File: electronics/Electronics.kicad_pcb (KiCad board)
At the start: 4 copper layers, 102.4 x 75 mm, 85 parts, among them J10 215079-4, J11 215079-4, J12 215079-4, J15 FTSH-105-XX-X-DV, J16 10118193-0001LF, J2 3mm_pad, J4 3mm_pad, J7 215079-4, J8 215079-4, J9 215079-4, Q1 BUK6Y10-30P, U1 STM32G441KBT3, U10 CM1223-02SO, U2 MAX14930DASE+, U3 MAX14930DASE+, U4 MAX14930DASE+, U5 DRV8243, U6 DRV8243, U7 DRV8243, U8 TPS54227DDAR, U9 NCP164

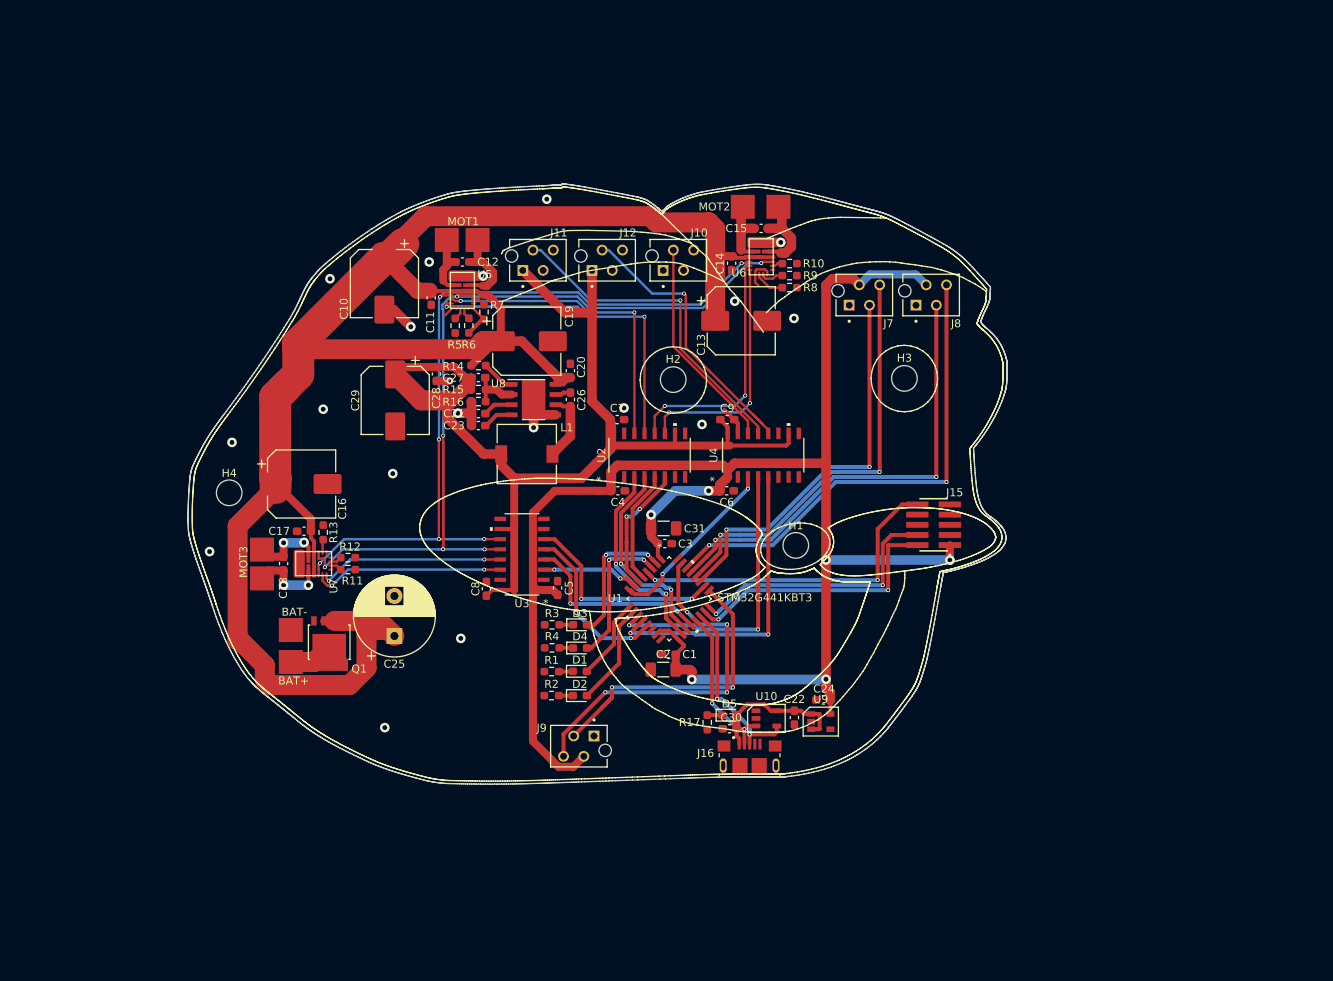
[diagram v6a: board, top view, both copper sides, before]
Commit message: Filled empty areas
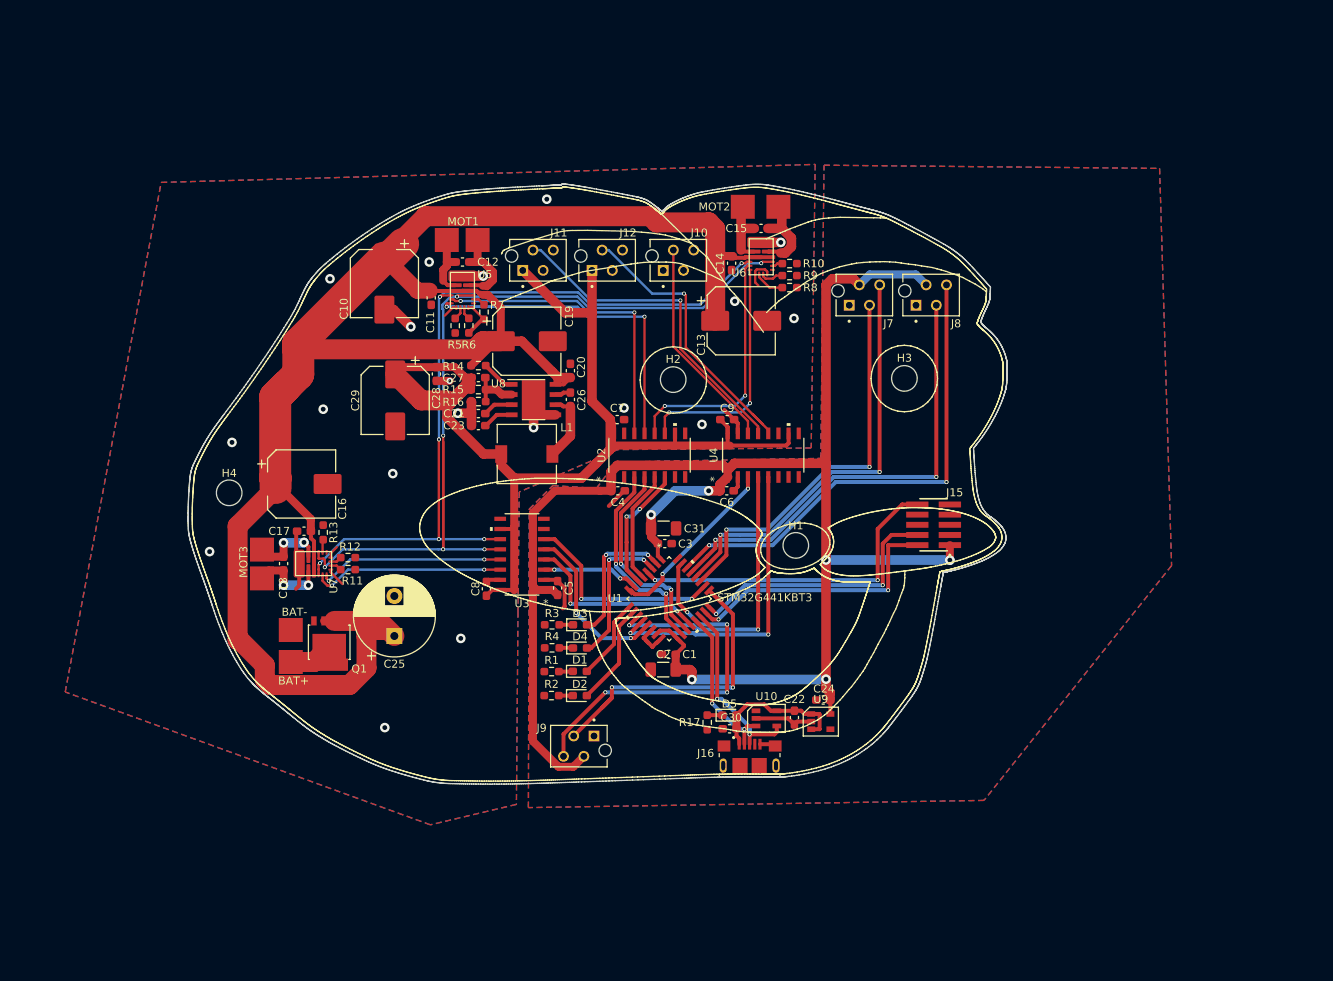
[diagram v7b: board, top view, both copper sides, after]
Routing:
- net GND: track 0.00 -> 24.6 mm
- net Earth: track 37.2 -> 50.6 mm
- added copper zone on B.Cu, net Earth
- added copper zone on F.Cu, net Earth
- added copper zone on B.Cu, net GND
- added copper zone on F.Cu, net GND
- added copper zone on In1.Cu, net GND
- added copper zone on In2.Cu, net GND
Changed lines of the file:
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@@
     (thickness 1.6)
     (drawings 11406)
-    (tracks 836)
+    (tracks 872)
     (zones 0)
     (modules 85)
@@
     (0 F.Cu signal)
     (1 In1.Cu signal)
-    (2 In2.Cu signal hide)
+    (2 In2.Cu signal)
     (31 B.Cu signal)
     (32 B.Adhes user)
@@
   (segment (start 70.284991 76.065009) (end 70.284991 72.265009) (width 4) (layer F.Cu) (net 1))
   (segment (start 67.4 78.95) (end 70.284991 76.065009) (width 4) (layer F.Cu) (net 1))
+  (segment (start 102.5375 101.775) (end 102.7 101.9375) (width 0.5) (layer F.Cu) (net 2))
+  (segment (start 100.974752 101.775) (end 102.5375 101.775) (width 0.5) (layer F.Cu) (net 2))
+  (segment (start 102.7 101.9375) (end 103.577008 102.814508) (width 0.5) (layer F.Cu) (net 2))
+  (segment (start 103.577008 102.814508) (end 103.577008 105.122992) (width 0.5) (layer F.Cu) (net 2))
+  (segment (start 103.577008 105.122992) (end 103.35 105.35) (width 0.5) (layer F.Cu) (net 2))
+  (segment (start 111.1 90.65) (end 111 90.65) (width 0.5) (layer F.Cu) (net 2))
+  (segment (start 111 90.65) (end 109.1 92.55) (width 0.5) (layer F.Cu) (net 2))
+  (segment (start 114.476672 108.020384) (end 113.45 109.047056) (width 0.5) (layer F.Cu) (net 2))
+  (segment (start 114.023526 109.620582) (end 114.023526 109.623526) (width 0.5) (layer F.Cu) (net 2))
+  (segment (start 115.139214 109.620582) (end 115.079418 109.620582) (width 0.5) (layer F.Cu) (net 2))
+  (segment (start 115.608042 109.151754) (end 115.139214 109.620582) (width 0.5) (layer F.Cu) (net 2))
+  (segment (start 115.079418 109.620582) (end 114.55 110.15) (width 0.5) (layer F.Cu) (net 2))
+  (segment (start 114.55 110.147056) (end 113.751472 109.348528) (width 0.5) (layer F.Cu) (net 2))
+  (segment (start 114.55 110.15) (end 114.55 110.147056) (width 0.5) (layer F.Cu) (net 2))
+  (segment (start 113.751472 109.348528) (end 114.023526 109.620582) (width 0.5) (layer F.Cu) (net 2))
+  (segment (start 113.45 109.047056) (end 113.751472 109.348528) (width 0.5) (layer F.Cu) (net 2))
+  (segment (start 125.225 90.1375) (end 124.7125 90.65) (width 0.5) (layer F.Cu) (net 2))
+  (segment (start 125.225 88.924752) (end 125.225 90.1375) (width 0.5) (layer F.Cu) (net 2))
+  (segment (start 129.675 122.325) (end 129.9 122.55) (width 0.5) (layer F.Cu) (net 2))
+  (segment (start 128 122.325) (end 129.675 122.325) (width 0.5) (layer F.Cu) (net 2))
+  (segment (start 131.5375 119.1) (end 132.3 119.8625) (width 0.5) (layer F.Cu) (net 2))
+  (segment (start 127.5 119.1) (end 131.5375 119.1) (width 0.5) (layer F.Cu) (net 2))
+  (segment (start 132.6625 119.5) (end 132.3 119.8625) (width 0.5) (layer F.Cu) (net 2))
+  (segment (start 134.4 119.5) (end 132.6625 119.5) (width 0.5) (layer F.Cu) (net 2))
   (segment (start 91.675 62.05) (end 92.65 62.05) (width 1) (layer F.Cu) (net 3))
   (segment (start 92.7 62) (end 92.7 59.3) (width 1) (layer F.Cu) (net 3))
@@
   (via (at 120.75 82.35) (size 1.2) (drill 0.6) (layers F.Cu B.Cu) (net 12))
   (segment (start 124.75 81.75) (end 123.55 80.55) (width 0.5) (layer F.Cu) (net 12))
+  (segment (start 70.022999 95.814501) (end 70.1375 95.7) (width 0.5) (layer F.Cu) (net 12))
+  (segment (start 70.022999 99.372999) (end 70.022999 95.814501) (width 0.5) (layer F.Cu) (net 12))
+  (segment (start 70.4 99.75) (end 70.022999 99.372999) (width 0.5) (layer F.Cu) (net 12))
+  (segment (start 70.4 99.75) (end 70.4 102.5) (width 0.5) (layer F.Cu) (net 12))
+  (segment (start 70.4 102.5) (end 70 102.9) (width 0.5) (layer F.Cu) (net 12))
+  (segment (start 74.35 99) (end 74.35 98.45) (width 0.3) (layer F.Cu) (net 12))
+  (segment (start 74.35 98.45) (end 75.1 97.7) (width 0.3) (layer F.Cu) (net 12))
+  (segment (start 74.35 100.5) (end 74.35 100.8) (width 0.3) (layer F.Cu) (net 12))
+  (segment (start 74.35 100.8) (end 74.35 100.85) (width 0.3) (layer F.Cu) (net 12))
+  (segment (start 74.35 100.85) (end 75.8 102.3) (width 0.3) (layer F.Cu) (net 12))
+  (segment (start 94.0625 101.775) (end 93.8 102.0375) (width 0.5) (layer F.Cu) (net 12))
+  (segment (start 95.525248 101.775) (end 94.0625 101.775) (width 0.5) (layer F.Cu) (net 12))
   (segment (start 109.755 82.2175) (end 109.2875 81.75) (width 0.5) (layer F.Cu) (net 14))
   (segment (start 109.755 83.475248) (end 109.755 82.2175) (width 0.5) (layer F.Cu) (net 14))
@@
       )
     )
+  )
+  (zone (net 12) (net_name Earth) (layer F.Cu) (hatch edge 0.508)
+    (connect_pads (clearance 0.508))
+    (min_thickness 0.254)
+    (fill yes (arc_segments 32) (thermal_gap 0.508) (thermal_bridge_width 0.508))
+    (polygon
+      (pts
+        (xy 134.4 85.3) (xy 110.2 85.5) (xy 97.9 90.8) (xy 97.75 105.75) (xy 97.55 129.85)
+        (xy 86.8 132.4) (xy 41.15 115.8) (xy 53.15 52.1) (xy 134.9 49.85)
+      )
+    )
+  )
+  (zone (net 12) (net_name Earth) (layer B.Cu) (hatch edge 0.508)
+    (connect_pads (clearance 0.508))
+    (min_thickness 0.254)
+    (fill yes (arc_segments 32) (thermal_gap 0.508) (thermal_bridge_width 0.508))
+    (polygon
+      (pts
+        (xy 134.4 85.3) (xy 110.2 85.5) (xy 97.9 90.8) (xy 97.75 105.75) (xy 97.55 129.85)
+        (xy 86.8 132.4) (xy 41.15 115.8) (xy 53.15 52.1) (xy 134.9 49.85)
+      )
+    )
+  )
+  (zone (net 2) (net_name GND) (layer In1.Cu) (hatch edge 0.508)
+    (connect_pads (clearance 0.508))
+    (min_thickness 0.254)
+    (fill yes (arc_segments 32) (thermal_gap 0.508) (thermal_bridge_width 0.508))
+    (polygon
+      (pts
+        (xy 177.95 50.35) (xy 179.45 100) (xy 156 129.35) (xy 99.05 130.25) (xy 99.15 92.95)
+        (xy 102.1 90) (xy 107.55 90.35) (xy 110 87.05) (xy 135.6 86.6) (xy 136 49.95)
+      )
+    )
+  )
+  (zone (net 2) (net_name GND) (layer F.Cu) (hatch edge 0.508)
+    (connect_pads (clearance 0.508))
+    (min_thickness 0.254)
+    (fill yes (arc_segments 32) (thermal_gap 0.508) (thermal_bridge_width 0.508))
+    (polygon
+      (pts
+        (xy 177.95 50.35) (xy 179.45 100) (xy 156 129.35) (xy 99.05 130.25) (xy 99.15 92.95)
+        (xy 102.1 90) (xy 107.55 90.35) (xy 110 87.05) (xy 135.6 86.6) (xy 136 49.95)
+      )
+    )
+  )
+  (zone (net 2) (net_name GND) (layer B.Cu) (hatch edge 0.508)
+    (connect_pads (clearance 0.508))
+    (min_thickness 0.254)
+    (fill yes (arc_segments 32) (thermal_gap 0.508) (thermal_bridge_width 0.508))
+    (polygon
+      (pts
+        (xy 177.95 50.35) (xy 179.45 100) (xy 156 129.35) (xy 99.05 130.25) (xy 99.15 92.95)
+        (xy 102.1 90) (xy 107.55 90.35) (xy 110 87.05) (xy 135.6 86.6) (xy 136 49.95)
+      )
+    )
+  )
+  (zone (net 2) (net_name GND) (layer In2.Cu) (hatch edge 0.508)
+    (connect_pads (clearance 0.508))
+    (min_thickness 0.254)
+    (fill yes (arc_segments 32) (thermal_gap 0.508) (thermal_bridge_width 0.508))
+    (polygon
+      (pts
+        (xy 177.95 50.35) (xy 179.45 100) (xy 156 129.35) (xy 99.05 130.25) (xy 99.15 92.95)
+        (xy 102.1 90) (xy 107.55 90.35) (xy 110 87.05) (xy 135.6 86.6) (xy 136 49.95)
+      )
+    )

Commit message: Rev2 Done?
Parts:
- moved J2 0.05 mm to (92.7, 59.4)
- moved MOT1 0.05 mm to (88.8, 59.4)
- renumbered J12 to Aim, J15 to Debug, J11 to Hold, J9 to MOT1, J7 to MOT1, J8 to MOT2, J10 to Thrower
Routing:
- net GND: vias 0 -> 20
- net Earth: vias 19 -> 27
- net /MCU-mot2-enc_2: vias 2 -> 3
- net /Driver/MOT1en_2: vias 2 -> 3
